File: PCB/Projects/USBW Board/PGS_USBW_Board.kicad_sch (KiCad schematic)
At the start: 45 parts, among them J1 Molex 505110-1792, J2 USB4056-03-A, J4 PH 2.0 JST, P1 RPI-RM2, Q1 BSS138DW, Q2 BSS138DW, U1 USBLC6-2P6, U2 USBLC6-2P6, U3 USBLC6-2P6, U4 TPS63001DRCR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

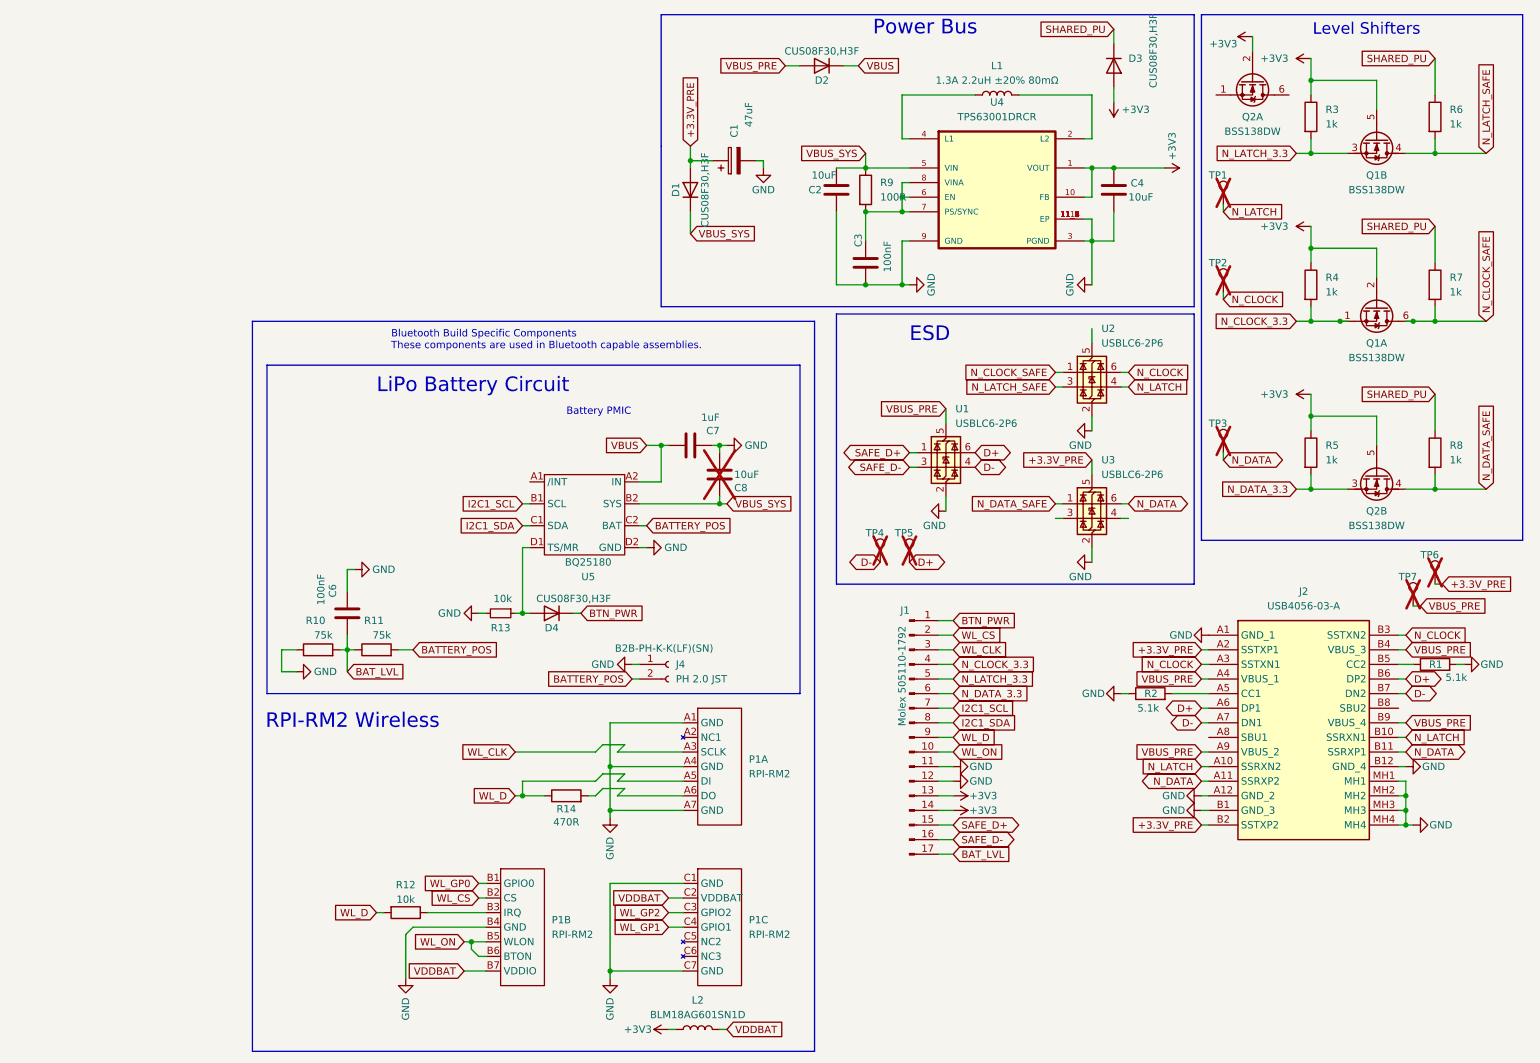
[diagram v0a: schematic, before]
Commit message: USBW Update
- Implement fuel gauge IC
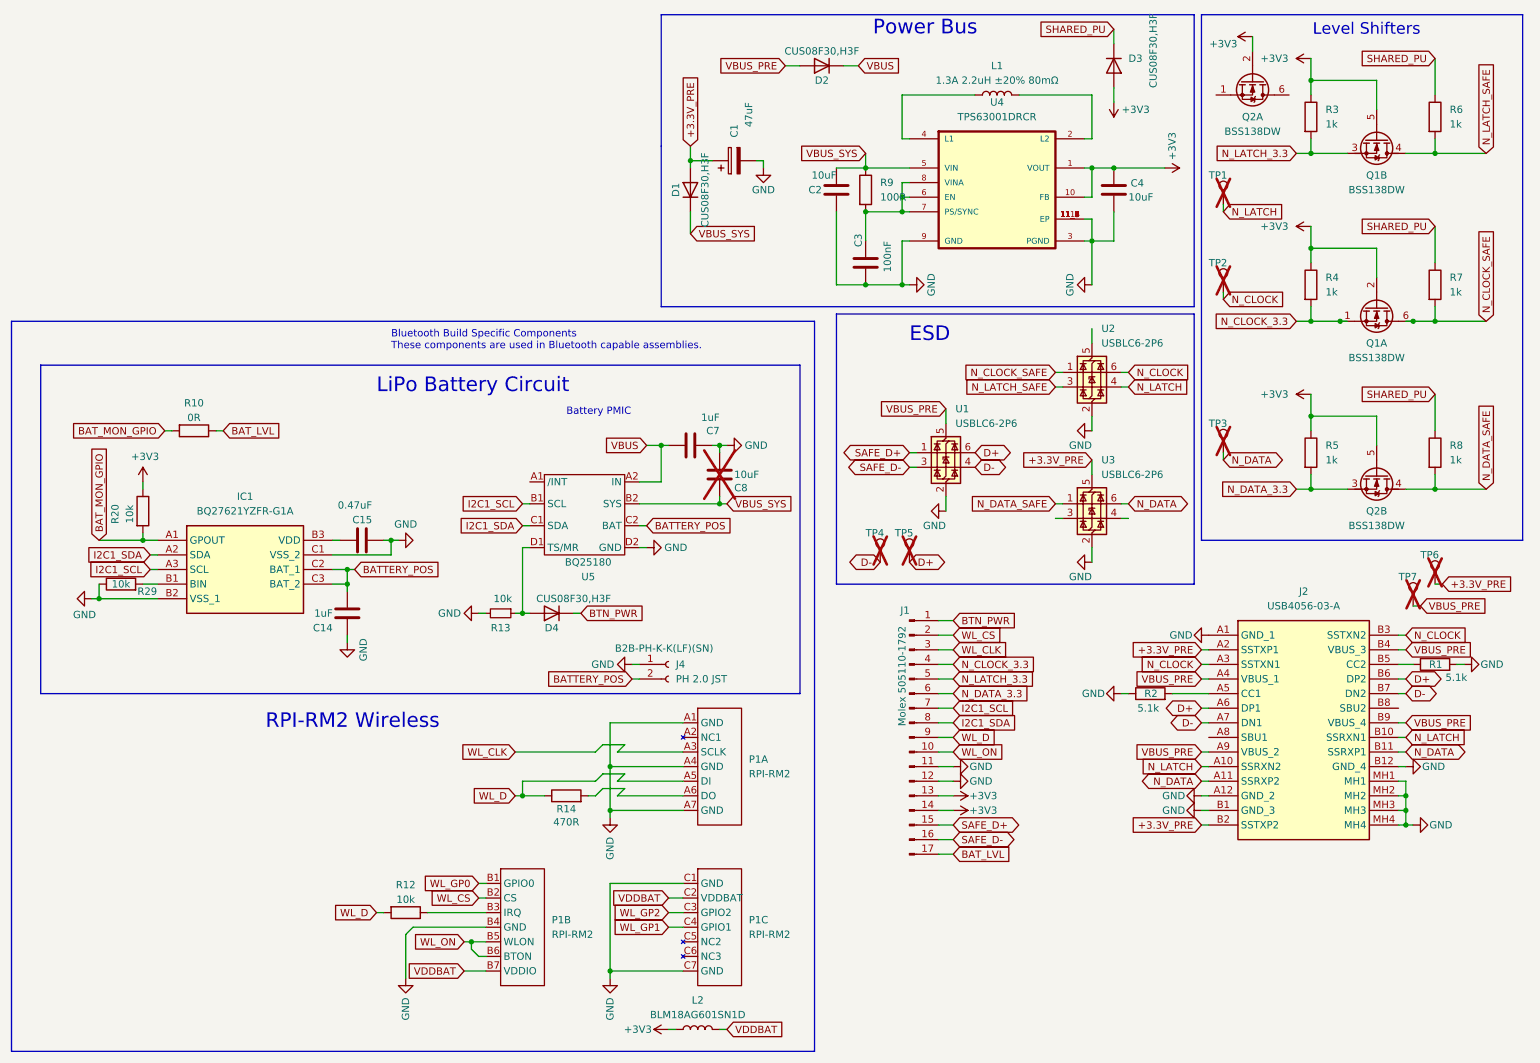
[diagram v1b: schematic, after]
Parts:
- removed C6: 100nF, Capacitor_SMD:C_0201_0603Metric, symbol Device:C
- removed R11: 75k, Resistor_SMD:R_0201_0603Metric, symbol Device:R
- added C14: 1uF, Capacitor_SMD:C_0201_0603Metric, symbol Device:C
- added C15: 0.47uF, Capacitor_SMD:C_0201_0603Metric, symbol Device:C
- added IC1: BQ27621YZFR-G1A, hhl:BGA9C50P3X3_162X158X62, symbol hhl:BQ27621YZFR-G1A
- added R20, R29: 10k, Resistor_SMD:R_0201_0603Metric, symbol Device:R
- D1, D2, D3, D4: value CUS08F30,H3F -> CUS08F30,H3F
- R10: value 75k -> 0R; Confirmed (none) -> YES; LCSC C2107901 -> C106227; Link (none) -> https://www.lcsc.com/product-detail/Chip-Resistor-Surface-M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; MPN AF0201FR-0775KL -> RC0201FR-070RL; Price 0.0006 -> 0.0005; Reviewed Yes -> (none); USBDNP YES -> (none)
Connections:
- net +3V3: now also R20.1
- net BATTERY_POS: now also C14.2, IC1.C2 (BAT_1), IC1.C3 (BAT_2)
- net BAT_LVL: now also R10.1; no longer R10.2
- net GND: now also C14.1, C15.2, IC1.B2 (VSS_1), IC1.C1 (VSS_2), R29.1; no longer R10.1
- net I2C1_SCL: now also IC1.A3 (SCL)
- net I2C1_SDA: now also IC1.A2 (SDA)
- new net: IC1.B1 (BIN), R29.2
- new net: C15.1, IC1.B3 (VDD)
- new net BAT_MON_GPIO: IC1.A1 (GPOUT), R10.2, R20.2

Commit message: Main Board/Trigger Board Update
- Main board updated with Kailh tactile switches
- Trigger board updated with Kailh tactile switches
- USBW board updated to remove unneeded diode, move position of USB-C port
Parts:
- removed D2: CUS08F30,H3F, Diode_SMD:D_SOD-323_HandSoldering, symbol hhl:CUS08F30
- C14, C15, IC1, R10, R20, R29: Reviewed (none) -> Yes
- P1: Reviewed Yes -> (none)
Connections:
- net VBUS_PRE is gone; now on net VBUS: J2.A4 (VBUS_1), J2.A9 (VBUS_2), J2.B4 (VBUS_3), J2.B9 (VBUS_4), TP7.1, U1.5 (VBUS)
